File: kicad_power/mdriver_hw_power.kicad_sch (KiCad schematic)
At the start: 18 parts, among them J1 Conn_02x05_Odd_Even, J2 Conn_01x02

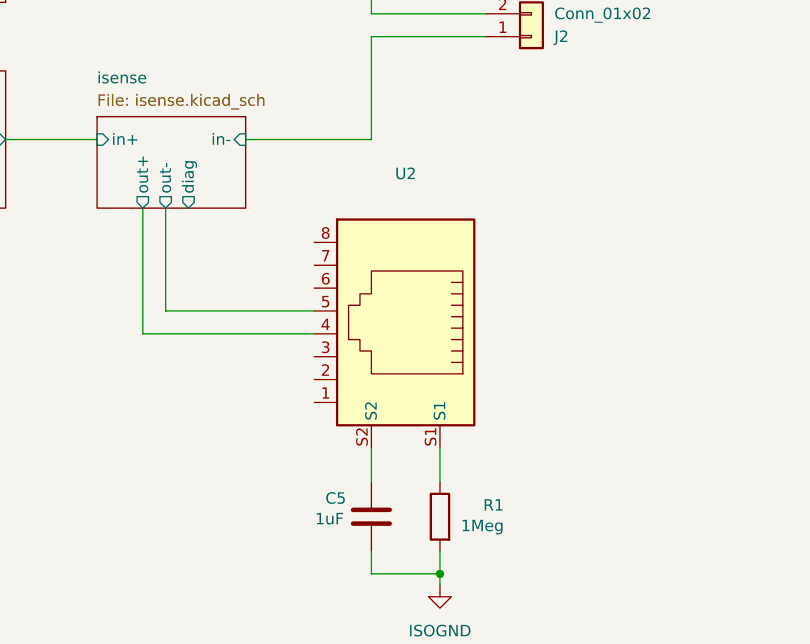
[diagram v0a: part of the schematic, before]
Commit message: finished initial layout of power stage in KiCAD
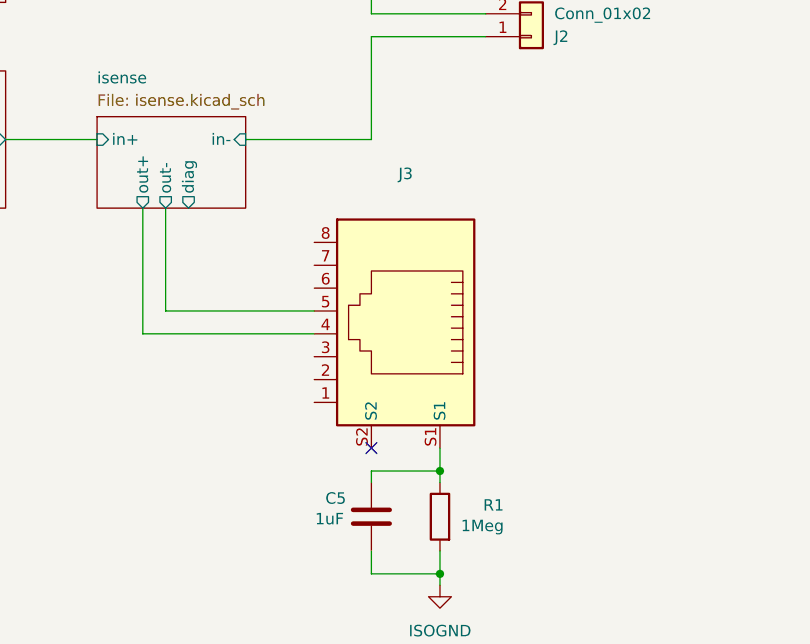
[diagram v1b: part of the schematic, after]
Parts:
- C5: Partno CC0603KRX7R7BB104 -> C0603C105K3RACTU
- F1, HS1, S1, S2, S3, S4, S5, S6: now left out of the parts list
- renumbered U2 to J3
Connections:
- net at C5.1: now also J3.S1, R1.1; no longer J3.S2
- no-connect marks 0 -> 1
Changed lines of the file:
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@@
+	)
+	(junction
+		(at 189.23 142.24)
+		(diameter 0)
+		(color 0 0 0 0)
 	)
 	(junction
@@
 		(color 0 0 0 0)
 	)
+	(no_connect
+		(at 181.61 139.7)
+	)
 	(wire
 		(pts
@@
 	(wire
 		(pts
+			(xy 181.61 142.24) (xy 189.23 142.24)
+		)
+		(stroke
+			(width 0)
+			(type default)
+		)
+	)
+	(wire
+		(pts
 			(xy 78.74 149.86) (xy 78.74 154.94)
 		)
@@
 	(wire
 		(pts
+			(xy 181.61 142.24) (xy 181.61 143.51)
+		)
+		(stroke
+			(width 0)
+			(type default)
+		)
+	)
+	(wire
+		(pts
 			(xy 140.97 82.55) (xy 181.61 82.55)
 		)
@@
 	(wire
 		(pts
-			(xy 181.61 139.7) (xy 181.61 143.51)
-		)
-		(stroke
-			(width 0)
-			(type default)
-		)
-	)
-	(wire
-		(pts
 			(xy 93.98 46.99) (xy 93.98 45.72)
 		)
@@
 	(wire
 		(pts
+			(xy 189.23 139.7) (xy 189.23 142.24)
+		)
+		(stroke
+			(width 0)
+			(type default)
+		)
+	)
+	(wire
+		(pts
 			(xy 156.21 127) (xy 156.21 113.03)
 		)
@@
 	(wire
 		(pts
-			(xy 189.23 139.7) (xy 189.23 143.51)
+			(xy 189.23 143.51) (xy 189.23 142.24)
 		)
 		(stroke
@@
 		(unit 1)
 		(exclude_from_sim no)
-		(in_bom yes)
+		(in_bom no)
 		(on_board yes)
 		(dnp no)
@@
 		(unit 1)
 		(exclude_from_sim no)
-		(in_bom yes)
+		(in_bom no)
 		(on_board yes)
 		(dnp no)
@@
 			)
 		)
-		(property "Description" "Unpolarized capacitor"
+		(property "Description" "Ceramic Capacitor, Multilayer, Ceramic, 25V, 10% +Tol, 10% -Tol, X7R, 15% TC, 1uF, Surface Mount, 0603"
 			(at 181.61 147.32 0)
 			(effects
@@
 			)
 		)
-		(property "Partno" "CC0603KRX7R7BB104"
+		(property "Partno" "C0603C105K3RACTU"
 			(at 181.61 147.32 0)
 			(effects
@@
 		(unit 1)
 		(exclude_from_sim no)
-		(in_bom yes)
+		(in_bom no)
 		(on_board yes)
 		(dnp no)
@@
 		(unit 1)
 		(exclude_from_sim no)
-		(in_bom yes)
+		(in_bom no)
 		(on_board yes)
 		(dnp no)
@@
 		(unit 1)
 		(exclude_from_sim no)
-		(in_bom yes)
+		(in_bom no)
 		(on_board yes)
 		(dnp no)
@@
 			)
 		)
-		(property "Description" "Resistor"
+		(property "Description" "63mW Thick Film Resistors 75V ±1% ±100ppm/℃ 1MΩ 0402 Chip Resistor - Surface Mount ROHS"
 			(at 189.23 147.32 0)
 			(effects
@@
 		(unit 1)
 		(exclude_from_sim no)
-		(in_bom yes)
+		(in_bom no)
 		(on_board yes)
 		(dnp no)
@@
 		(dnp no)
 		(fields_autoplaced yes)
-		(property "Reference" "U2"
+		(property "Reference" "J3"
 			(at 185.42 109.22 0)
 			(effects
@@
 			)
 		)
-		(property "Datasheet" ""
+		(property "Datasheet" "https://octopart.com/datasheet/634008149821-wurth+elektronik-52676018"
 			(at 185.42 125.73 0)
 			(effects
@@
 			)
 		)
-		(property "Description" ""
+		(property "Description" "Modular Jack WR-MJ, Tab Up, Shielded, Horizontal Entry, SMT, 8P8C"
 			(at 185.42 125.73 0)
 			(effects
@@
 			(project ""
 				(path "/b0a218b5-3684-447f-8dec-1dd61a8887f1"
-					(reference "U2")
+					(reference "J3")
 					(unit 1)
 				)
@@
 		(unit 1)
 		(exclude_from_sim no)
-		(in_bom yes)
+		(in_bom no)
 		(on_board yes)
 		(dnp no)
@@
 		(unit 1)
 		(exclude_from_sim no)
-		(in_bom yes)
+		(in_bom no)
 		(on_board yes)
 		(dnp no)

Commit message: adjustment to PCB layout, created BOM file, added MOSFET gate discharge diodes
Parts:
- F1, HS1, S1, S2, S3, S4, S5, S6: now in the parts list
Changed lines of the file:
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@@
 		(unit 1)
 		(exclude_from_sim no)
-		(in_bom no)
+		(in_bom yes)
 		(on_board yes)
 		(dnp no)
@@
 		(unit 1)
 		(exclude_from_sim no)
-		(in_bom no)
+		(in_bom yes)
 		(on_board yes)
 		(dnp no)
@@
 		(unit 1)
 		(exclude_from_sim no)
-		(in_bom no)
+		(in_bom yes)
 		(on_board yes)
 		(dnp no)
@@
 		(unit 1)
 		(exclude_from_sim no)
-		(in_bom no)
+		(in_bom yes)
 		(on_board yes)
 		(dnp no)
@@
 		(unit 1)
 		(exclude_from_sim no)
-		(in_bom no)
+		(in_bom yes)
 		(on_board yes)
 		(dnp no)
@@
 		(unit 1)
 		(exclude_from_sim no)
-		(in_bom no)
+		(in_bom yes)
 		(on_board yes)
 		(dnp no)
@@
 		(unit 1)
 		(exclude_from_sim no)
-		(in_bom no)
+		(in_bom yes)
 		(on_board yes)
 		(dnp no)
@@
 		(unit 1)
 		(exclude_from_sim no)
-		(in_bom no)
-		(on_board yes)
-		(dnp no)
+		(in_bom yes)
+		(on_board yes)
+		(dnp no)

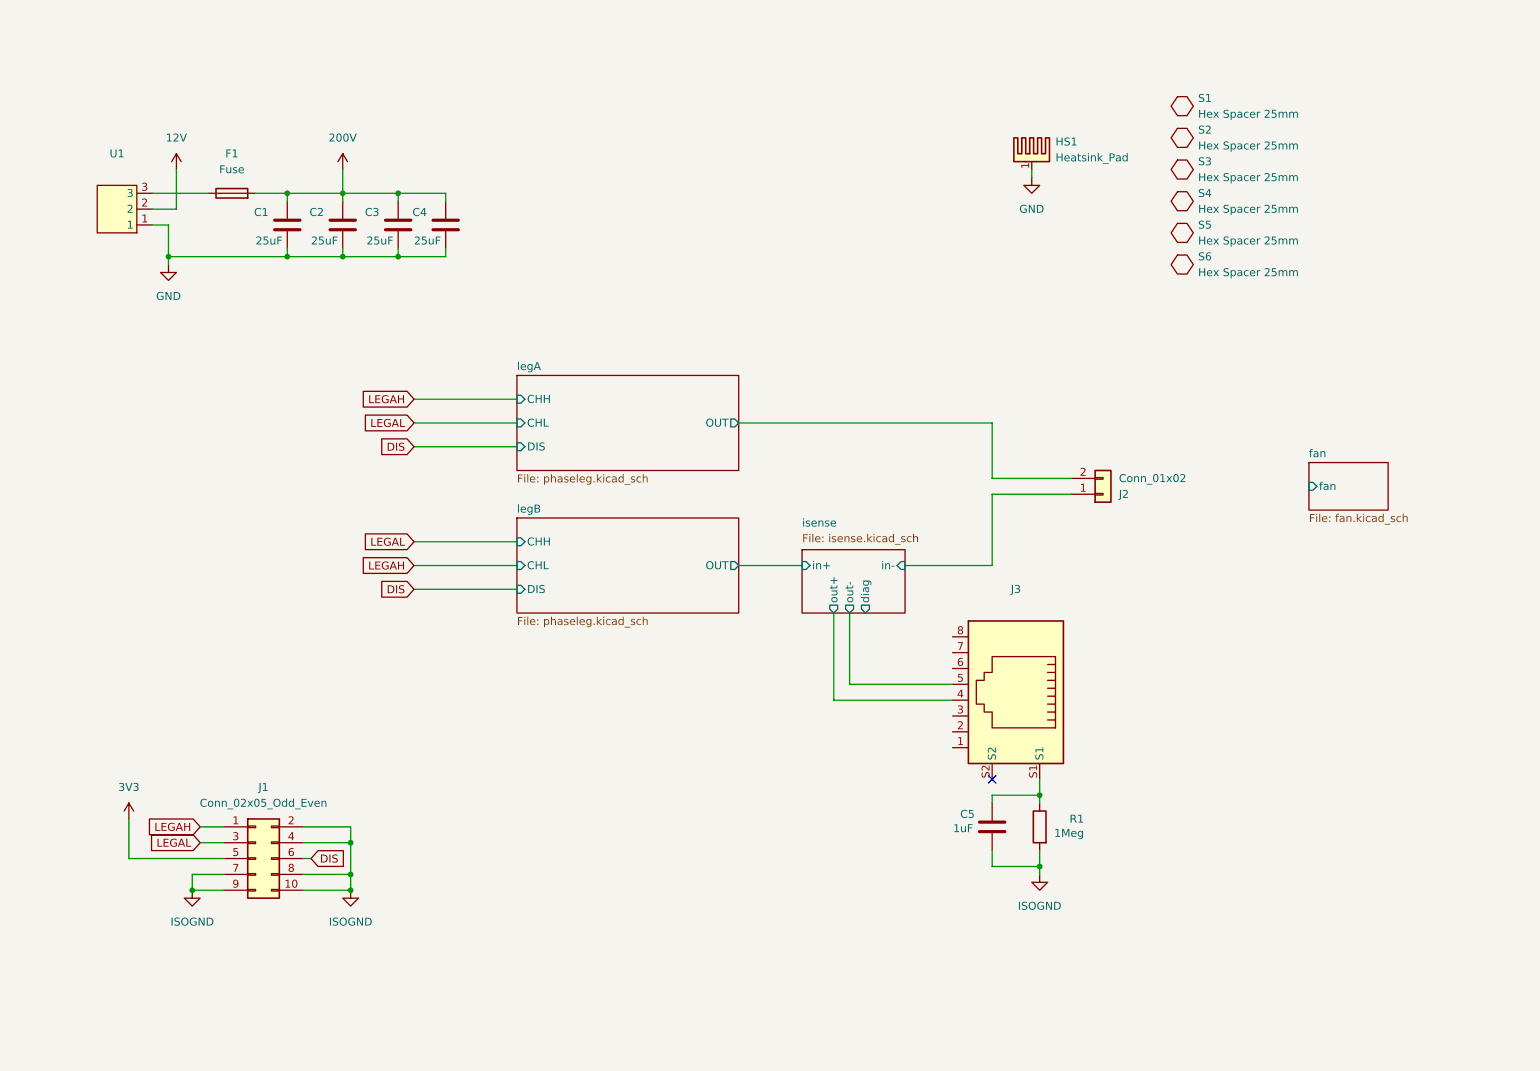
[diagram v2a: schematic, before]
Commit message: introduced AGND and A3V3, ensures HV design rules
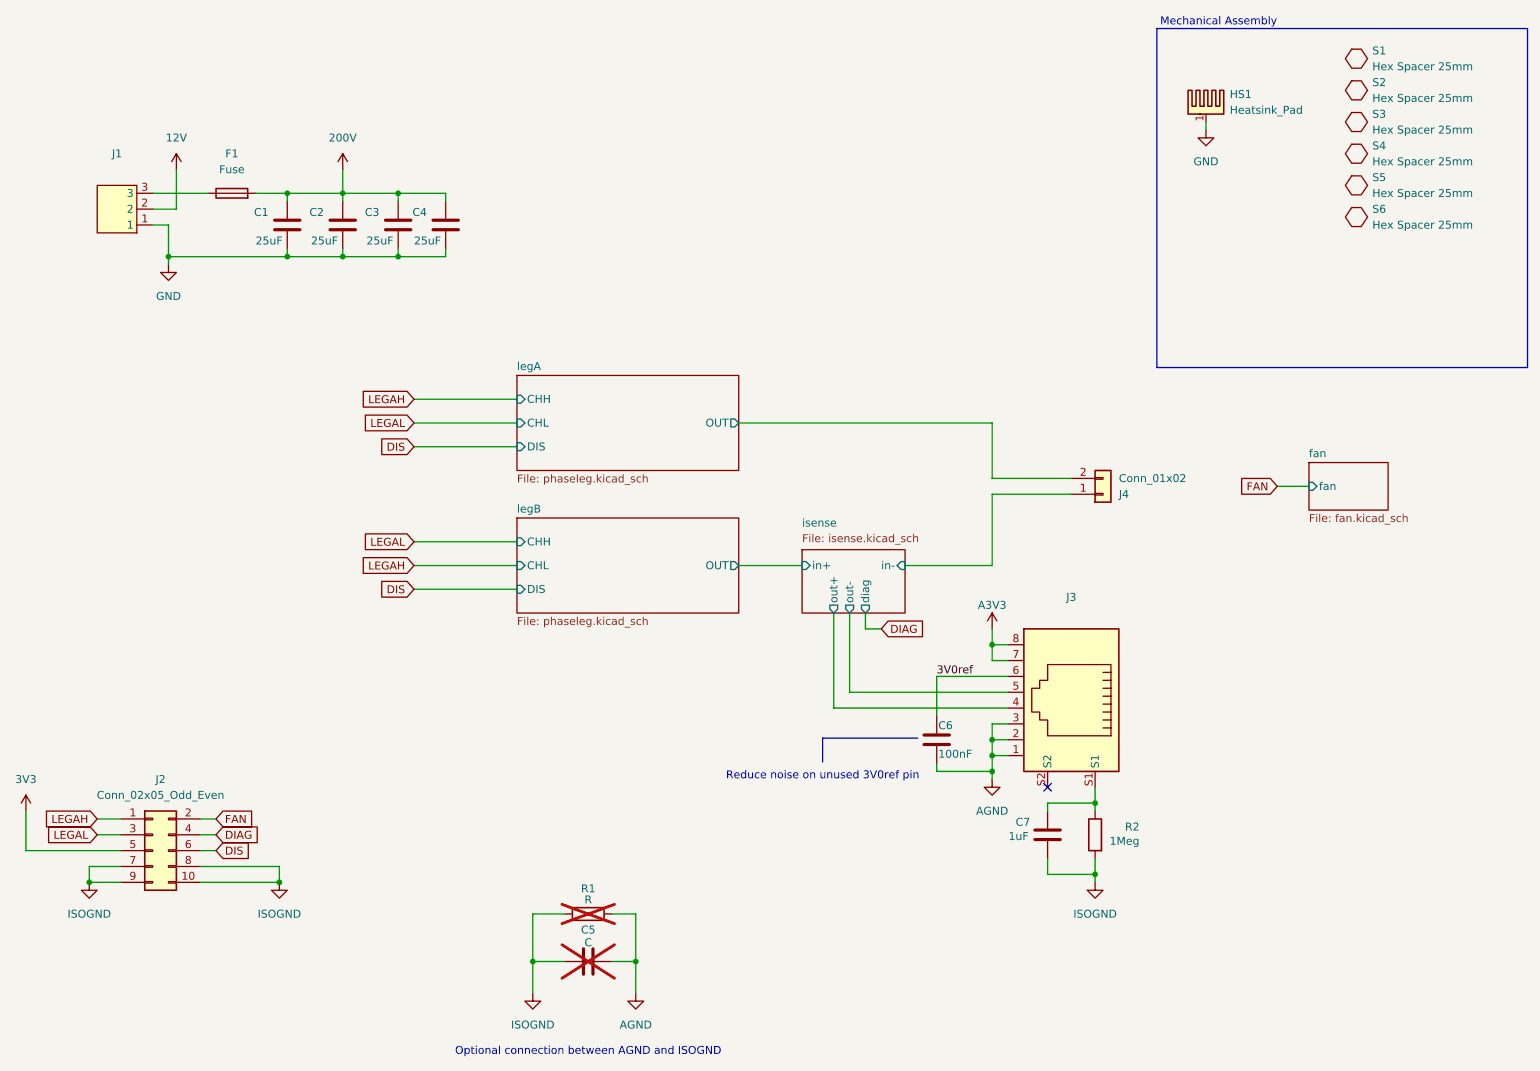
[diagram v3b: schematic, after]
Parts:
- added C5: C, Capacitor_SMD:C_0402_1005Metric, symbol Device:C
- added C6: 100nF, Capacitor_SMD:C_0402_1005Metric, symbol Device:C
- added R1: R, Resistor_SMD:R_0402_1005Metric, symbol Device:R
- C1, C2, C3, C4, HS1, S1, S2, S3, S4, S5, S6: now left out of the parts list
- J1: renamed from U1; now left out of the parts list
- J4: renamed from J2; now left out of the parts list
- renumbered C5 to C7, J1 to J2, R1 to R2
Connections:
- net ISOGND: now also C5.1, R1.1; no longer J2.2 (Pin_2), J2.4 (Pin_4)
- net AGND: now reaches J3.1
- net AGND: now also J3.2, J3.3, C5.2, C6.2, R1.2
- net 3V0ref: now reaches J3.6
- net 3V0ref: now also C6.1
- net A3V3: now reaches J3.7
- net A3V3: now also J3.8
- new net DIAG: J2.4 (Pin_4)
- new net FAN: J2.2 (Pin_2)
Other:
- note added: "Mechanical Assembly"
- note added: "Optional connection between AGND and ISOGND"
- note added: "Reduce noise on unused 3V0ref pin"
- moved on the sheet: C7, HS1, J2, J3, R2, S1, S2, S3, S4, S5, S6

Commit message: finished version 1.1 of power board
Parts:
- added R26, R27: 68k, Resistor_SMD:R_2512_6332Metric, symbol Device:R
- C1, C2, C3, C4, F1, HS1, J1, J2, J3, J4, S1, S2, S3, S4, S5, S6: JLCPCB (none) -> -
- C5, R1: JLCPCB (none) -> -; Partno (none) -> -
- C6: JLCPCB (none) -> C1525
- C7: value 1uF -> 2.2u; JLCPCB (none) -> CL10A225KA8NNNC; Partno C0603C105K3RACTU -> CGA3E1X7S1C225K080AE
- R2: JLCPCB (none) -> C26083
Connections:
- net 200V: now also R26.1, R27.1
- net 3V0ref: now also J3.3; no longer J3.6
- net A3V3: now also J3.1, J3.2; no longer J3.7, J3.8
- net AGND: now also J3.6, J3.7, J3.8; no longer J3.1, J3.2, J3.3
- net GND: now also R26.2, R27.2
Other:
- note added: "tau ~= 3.4s P ~= 1.17W < 4W"
- moved on the sheet: J3, R2
